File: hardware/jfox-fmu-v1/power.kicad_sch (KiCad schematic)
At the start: 7 parts, among them U20 LTC4417CGN, U21 AP2112K-3.3, U22 AP2112K-3.3, U23 AP22804AW5, U24 AP22804AW5, U25 AP22804AW5, U26 AP22804AW5

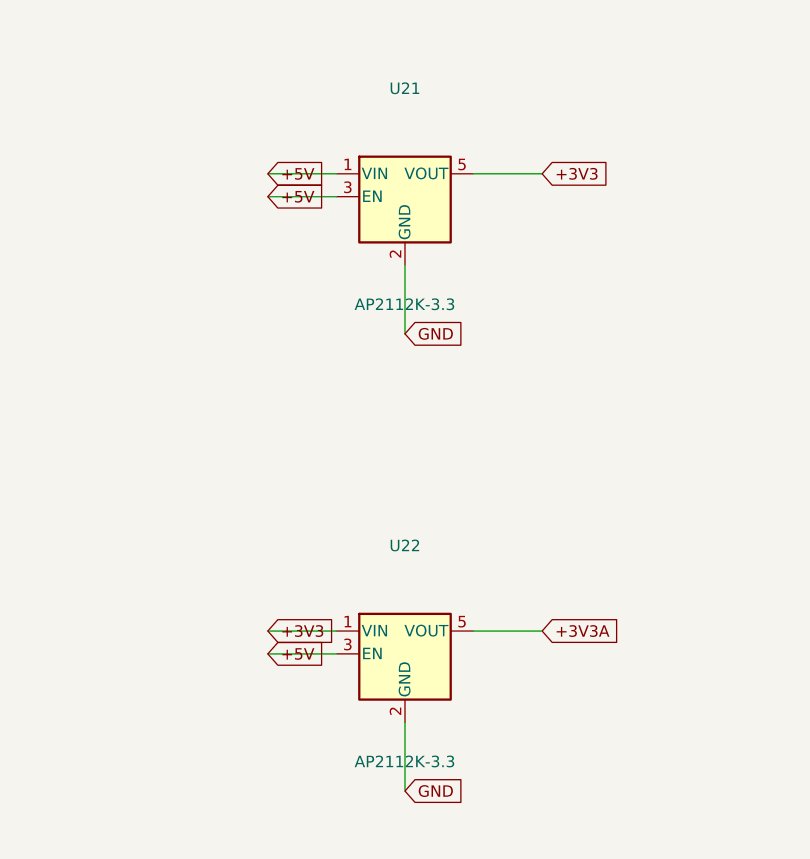
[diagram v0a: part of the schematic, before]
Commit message: Fix the derived-symbol cache; assemble the sheets into one project
The power sheet's 28 unconnected wire endpoints and 19 dangling labels are
gone, and the cause was not the geometry - that was right all along.

KiCad symbols like AP2112K-3.3 and AP22804AW5 `(extends ...)` a base part and
carry no drawing of their own. A schematic's lib_symbols cache cannot express
that: the parent gets cached under its prefixed name while the child still
refers to it by its bare one, so the reference dangles, KiCad resolves no
pins, and every wire drawn to where the pins should be reports as an
unconnected endpoint. The fix is to flatten the way KiCad does when it caches
- keep the derived symbol's own properties, since its part number is the
whole point, and graft in the parent's graphics and pins.

Two attempts failed silently before that worked, both for the same reason:
patterns anchored on a fixed indent. _one_sym re-indents by a tab, so
`\n\t\t\(extends` matched nothing against three tabs, and the flatten quietly
did not happen. Both are indent-agnostic and paren-counted now.

Also adds the project root. Until it existed each sheet was a separate
project as far as KiCad was concerned, so a global label on the power sheet
could not reach the MCU sheet and ERC reported both ends as isolated. The
nets were right; the project simply was not assembled. Four sheets now
enumerate as one design.

check_fmu_schematic gains the power tree's load-bearing properties: each
sensor rail must come from its own load switch, or "power-cycle the wedged
IMU" quietly means "power-cycle two working ones as well"; and the ORing
controller's three inputs must stay distinct.

That check was wrong on its first run and reported the schematic as broken.
It compared bare reference designators, and on a sheet where only the
LTC4417 exists all three inputs touch U20, so they looked identical. Fixed to
compare (ref, pin) pairs. Worth recording: a checker that cries wolf is worse
than no checker, because the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
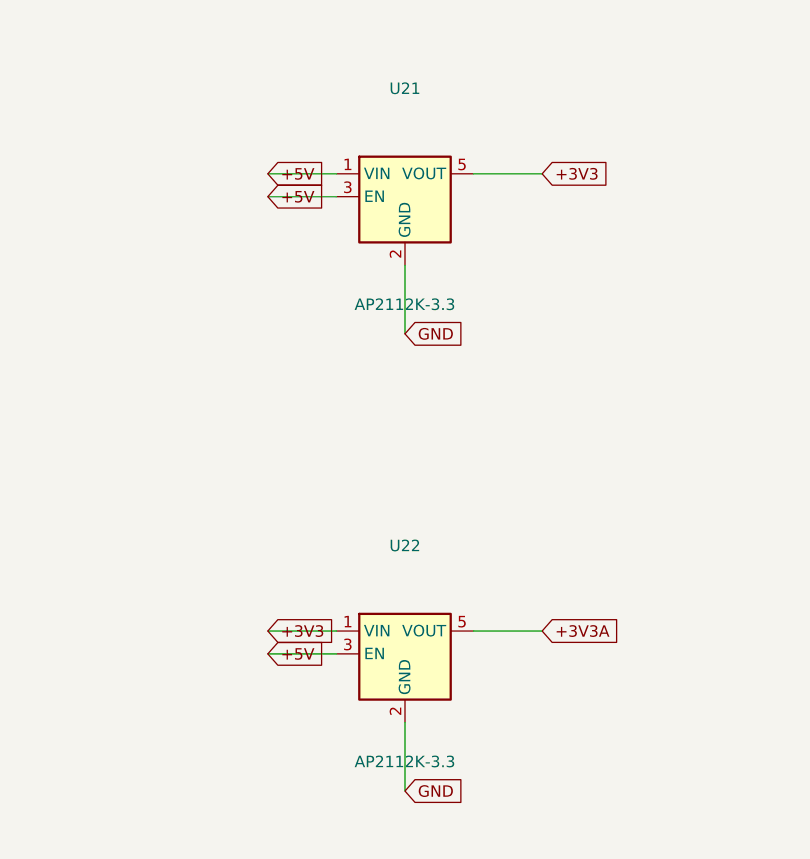
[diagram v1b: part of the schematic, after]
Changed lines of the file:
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@@
 		(instances
 			(project "jfox-fmu"
-				(path "/b6c9b46f-eb78-4010-a417-3db569aedb31"
+				(path "/8405edfd-9bd5-42f1-af2e-149ab58af58f"
 					(reference "U20")
 					(unit 1)
@@
 		(instances
 			(project "jfox-fmu"
-				(path "/b6c9b46f-eb78-4010-a417-3db569aedb31"
+				(path "/8405edfd-9bd5-42f1-af2e-149ab58af58f"
 					(reference "U21")
 					(unit 1)
@@
 		(instances
 			(project "jfox-fmu"
-				(path "/b6c9b46f-eb78-4010-a417-3db569aedb31"
+				(path "/8405edfd-9bd5-42f1-af2e-149ab58af58f"
 					(reference "U22")
 					(unit 1)
@@
 		(instances
 			(project "jfox-fmu"
-				(path "/b6c9b46f-eb78-4010-a417-3db569aedb31"
+				(path "/8405edfd-9bd5-42f1-af2e-149ab58af58f"
 					(reference "U23")
 					(unit 1)
@@
 		(instances
 			(project "jfox-fmu"
-				(path "/b6c9b46f-eb78-4010-a417-3db569aedb31"
+				(path "/8405edfd-9bd5-42f1-af2e-149ab58af58f"
 					(reference "U24")
 					(unit 1)
@@
 		(instances
 			(project "jfox-fmu"
-				(path "/b6c9b46f-eb78-4010-a417-3db569aedb31"
+				(path "/8405edfd-9bd5-42f1-af2e-149ab58af58f"
 					(reference "U25")
 					(unit 1)
@@
 		(instances
 			(project "jfox-fmu"
-				(path "/b6c9b46f-eb78-4010-a417-3db569aedb31"
+				(path "/8405edfd-9bd5-42f1-af2e-149ab58af58f"
 					(reference "U26")
 					(unit 1)

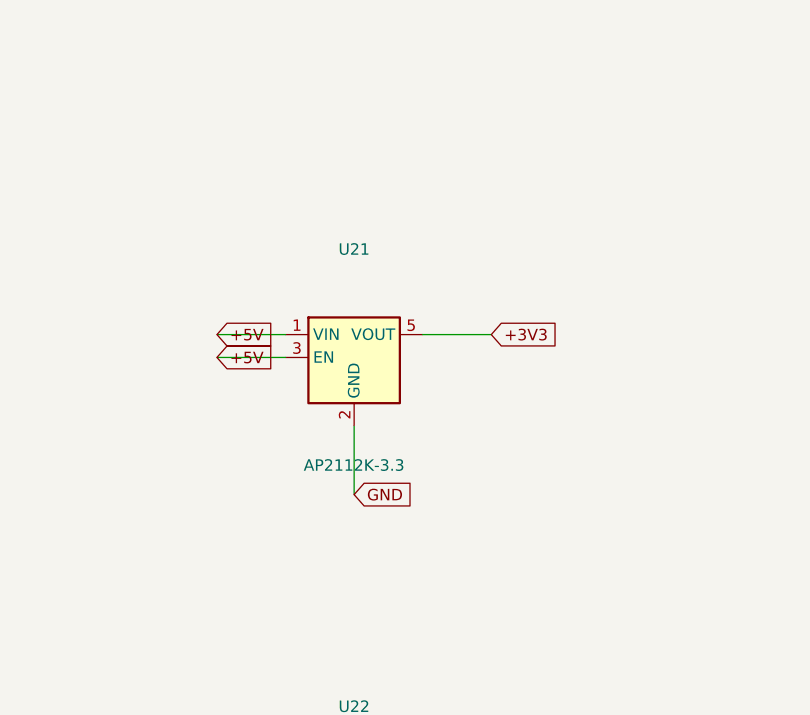
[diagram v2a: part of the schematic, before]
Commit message: Settle the regulator questions from ST's datasheet; U21 becomes a buck
Two separate "LDO or not" questions had been left open. Both are now answered
from the manufacturer's datasheet rather than from inference, and one of them
changes the design.

The MCU's internal regulator is the LDO, and not by preference. ST's
STM32H753xI datasheet states that Scale 0 - boosted performance - is
"available only with LDO regulator", and 480 MHz requires VOS0. So the two
VCAP pins and their 2.2 uF are right, and the SMPS option is simply
unavailable to this design at this clock. The earlier note reasoned from
KiCad's symbol exposing no SMPS pins and reached the right answer for a weak
reason; this is the real one. The same datasheet also confirms LQFP176 is a
real package for this part, which had only been taken from the symbol library.

The board's 5 V to 3V3 converter is a different question, and the answer is
different. POWER_BUDGET.md puts the 3V3 load at ~310 mA typical and ~550 mA
peak, built from ST's Table 20 for the MCU and the sensor datasheets for the
rest. An LDO dropping 1.7 V across that burns 0.53 to 0.94 W, and an SOT-23-5
at roughly 250 C/W would need a 130 C rise to shed it. The AP2112K-3.3 first
drawn there was not marginal, it was wrong by a factor of several. U21 is now
a TPS62130 synchronous buck, which dissipates about 35 mW instead.

U22 stays an LDO deliberately. It carries only VDDA and VREF+, a few mA, and
a linear regulator is the right choice there precisely because it is quiet -
putting the analog rail behind the switcher that feeds the digital load would
inject its ripple into the ADC reference.

The budget records its own weak point rather than hiding it: ST's rev Y tables
stop at 400 MHz, so there is no published VOS0 figure at 480 MHz and the
budget uses the 400 MHz number. The real current is therefore higher than
stated, which only strengthens the conclusion.

All six schematic checks still pass.

Co-Authored-By: Claude Opus 5 <noreply@anthropic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
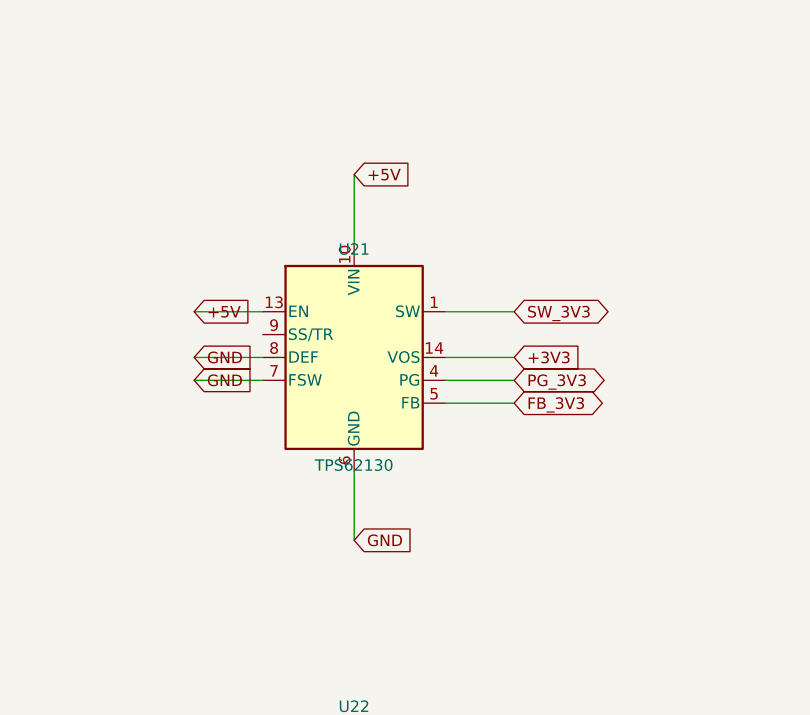
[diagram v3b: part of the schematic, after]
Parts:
- removed U21: AP2112K-3.3, symbol Regulator_Linear:AP2112K-3.3
- added U21: TPS62130, symbol Regulator_Switching:TPS62130
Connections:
- net +3V3: now also U21.14 (VOS)
- net +5V: now also U21.10 (VIN), U21.11 (VIN), U21.12 (VIN), U21.13 (EN)
- net GND: now also U21.15 (GND), U21.16 (GND), U21.17 (GND), U21.6 (GND), U21.7 (FSW), U21.8 (DEF)
- new net FB_3V3: U21.5 (FB)
- new net PG_3V3: U21.4 (PG)
- new net SW_3V3: U21.1 (SW), U21.2 (SW), U21.3 (SW)
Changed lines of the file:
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@@
 		(instances
 			(project "jfox-fmu"
-				(path "/eb04d008-9f2c-4c3f-a242-364287b3839a"
+				(path "/824115a0-8493-41a1-9e91-3339ab024d2c"
 					(reference "U20")
 					(unit 1)
@@
 	)
 	(symbol
-		(lib_id "Regulator_Linear:AP2112K-3.3")
+		(lib_id "Regulator_Switching:TPS62130")
 		(at 177.8 63.5 0)
 		(unit 1)
@@
 		)
 		)
-		(property "Value" "AP2112K-3.3"
+		(property "Value" "TPS62130"
 			(at 177.8 75.5 0)
 			(effects
@@
 		(instances
 			(project "jfox-fmu"
-				(path "/eb04d008-9f2c-4c3f-a242-364287b3839a"
+				(path "/824115a0-8493-41a1-9e91-3339ab024d2c"
 					(reference "U21")
 					(unit 1)
@@
 	(wire
 		(pts
-			(xy 170.18 60.96) (xy 162.56 60.96)
+			(xy 187.96 58.42) (xy 195.58 58.42)
+		)
+		(stroke
+			(width 0)
+			(type default)
+		)
+	)
+	(global_label "SW_3V3"
+		(shape bidirectional)
+		(at 195.58 58.42 180)
+		(fields_autoplaced yes)
+		(effects
+			(font
+				(size 1.27 1.27)
+			)
+			(justify left)
+		)
+	)
+	(wire
+		(pts
+			(xy 187.96 66.04) (xy 195.58 66.04)
+		)
+		(stroke
+			(width 0)
+			(type default)
+		)
+	)
+	(global_label "PG_3V3"
+		(shape bidirectional)
+		(at 195.58 66.04 180)
+		(fields_autoplaced yes)
+		(effects
+			(font
+				(size 1.27 1.27)
+			)
+			(justify left)
+		)
+	)
+	(wire
+		(pts
+			(xy 187.96 68.58) (xy 195.58 68.58)
+		)
+		(stroke
+			(width 0)
+			(type default)
+		)
+	)
+	(global_label "FB_3V3"
+		(shape bidirectional)
+		(at 195.58 68.58 180)
+		(fields_autoplaced yes)
+		(effects
+			(font
+				(size 1.27 1.27)
+			)
+			(justify left)
+		)
+	)
+	(wire
+		(pts
+			(xy 177.8 76.2) (xy 177.8 83.82)
+		)
+		(stroke
+			(width 0)
+			(type default)
+		)
+	)
+	(global_label "GND"
+		(shape input)
+		(at 177.8 83.82 180)
+		(fields_autoplaced yes)
+		(effects
+			(font
+				(size 1.27 1.27)
+			)
+			(justify left)
+		)
+	)
+	(wire
+		(pts
+			(xy 167.64 66.04) (xy 160.02 66.04)
+		)
+		(stroke
+			(width 0)
+			(type default)
+		)
+	)
+	(global_label "GND"
+		(shape input)
+		(at 160.02 66.04 0)
+		(fields_autoplaced yes)
+		(effects
+			(font
+				(size 1.27 1.27)
+			)
+			(justify left)
+		)
+	)
+	(wire
+		(pts
+			(xy 167.64 63.5) (xy 160.02 63.5)
+		)
+		(stroke
+			(width 0)
+			(type default)
+		)
+	)
+	(global_label "GND"
+		(shape input)
+		(at 160.02 63.5 0)
+		(fields_autoplaced yes)
+		(effects
+			(font
+				(size 1.27 1.27)
+			)
+			(justify left)
+		)
+	)
+	(wire
+		(pts
+			(xy 177.8 50.8) (xy 177.8 43.18)
 		)
 		(stroke
@@
 	(global_label "+5V"
 		(shape input)
-		(at 162.56 60.96 0)
-		(fields_autoplaced yes)
-		(effects
-			(font
-				(size 1.27 1.27)
-			)
-			(justify left)
-		)
-	)
-	(wire
-		(pts
-			(xy 177.8 71.12) (xy 177.8 78.74)
-		)
-		(stroke
-			(width 0)
-			(type default)
-		)
-	)
-	(global_label "GND"
-		(shape input)
-		(at 177.8 78.74 180)
-		(fields_autoplaced yes)
-		(effects
-			(font
-				(size 1.27 1.27)
-			)
-			(justify left)
-		)
-	)
-	(wire
-		(pts
-			(xy 170.18 63.5) (xy 162.56 63.5)
+		(at 177.8 43.18 180)
+		(fields_autoplaced yes)
+		(effects
+			(font
+				(size 1.27 1.27)
+			)
+			(justify left)
+		)
+	)
+	(wire
+		(pts
+			(xy 167.64 58.42) (xy 160.02 58.42)
 		)
 		(stroke
@@
 	(global_label "+5V"
 		(shape input)
-		(at 162.56 63.5 0)
-		(fields_autoplaced yes)
-		(effects
-			(font
-				(size 1.27 1.27)
-			)
-			(justify left)
-		)
-	)
-	(wire
-		(pts
-			(xy 185.42 60.96) (xy 193.04 60.96)
+		(at 160.02 58.42 0)
+		(fields_autoplaced yes)
+		(effects
+			(font
+				(size 1.27 1.27)
+			)
+			(justify left)
+		)
+	)
+	(wire
+		(pts
+			(xy 187.96 63.5) (xy 195.58 63.5)
 		)
 		(stroke
@@
 	(global_label "+3V3"
 		(shape input)
-		(at 193.04 60.96 180)
+		(at 195.58 63.5 180)
 		(fields_autoplaced yes)
 		(effects
@@
 		(instances
 			(project "jfox-fmu"
-				(path "/eb04d008-9f2c-4c3f-a242-364287b3839a"
+				(path "/824115a0-8493-41a1-9e91-3339ab024d2c"
 					(reference "U22")
 					(unit 1)
@@
 		(instances
 			(project "jfox-fmu"
-				(path "/eb04d008-9f2c-4c3f-a242-364287b3839a"
+				(path "/824115a0-8493-41a1-9e91-3339ab024d2c"
 					(reference "U23")
 					(unit 1)
@@
 		(instances
 			(project "jfox-fmu"
-				(path "/eb04d008-9f2c-4c3f-a242-364287b3839a"
+				(path "/824115a0-8493-41a1-9e91-3339ab024d2c"
 					(reference "U24")
 					(unit 1)
@@
 		(instances
 			(project "jfox-fmu"
-				(path "/eb04d008-9f2c-4c3f-a242-364287b3839a"
+				(path "/824115a0-8493-41a1-9e91-3339ab024d2c"
 					(reference "U25")
 					(unit 1)
@@
 		(instances
 			(project "jfox-fmu"
-				(path "/eb04d008-9f2c-4c3f-a242-364287b3839a"
+				(path "/824115a0-8493-41a1-9e91-3339ab024d2c"
 					(reference "U26")
 					(unit 1)
